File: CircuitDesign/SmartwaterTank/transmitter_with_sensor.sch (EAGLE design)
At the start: 11 parts, among them IC1 MEGA8-P

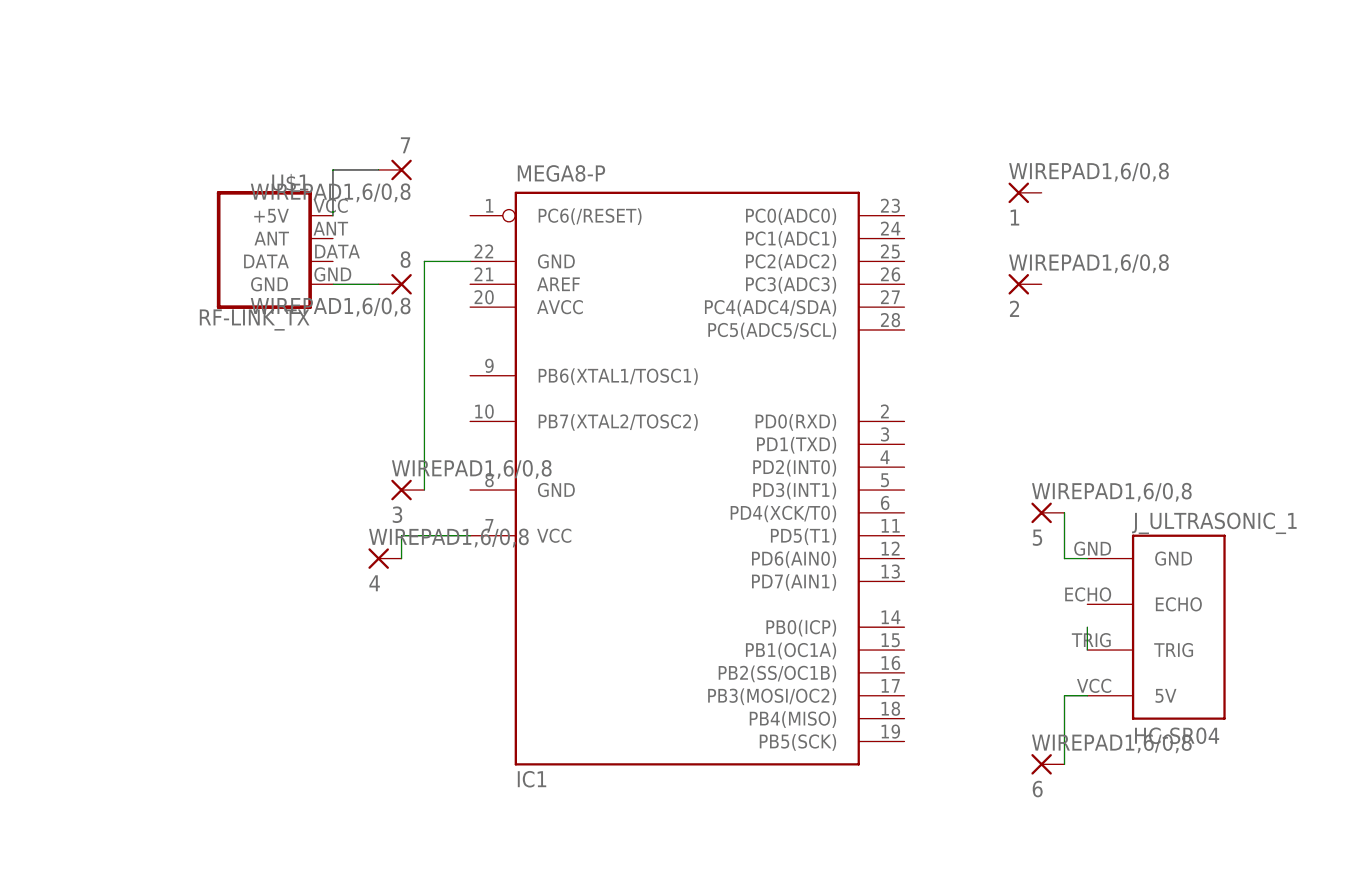
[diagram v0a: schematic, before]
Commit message: Issue #5: update transmitter schema
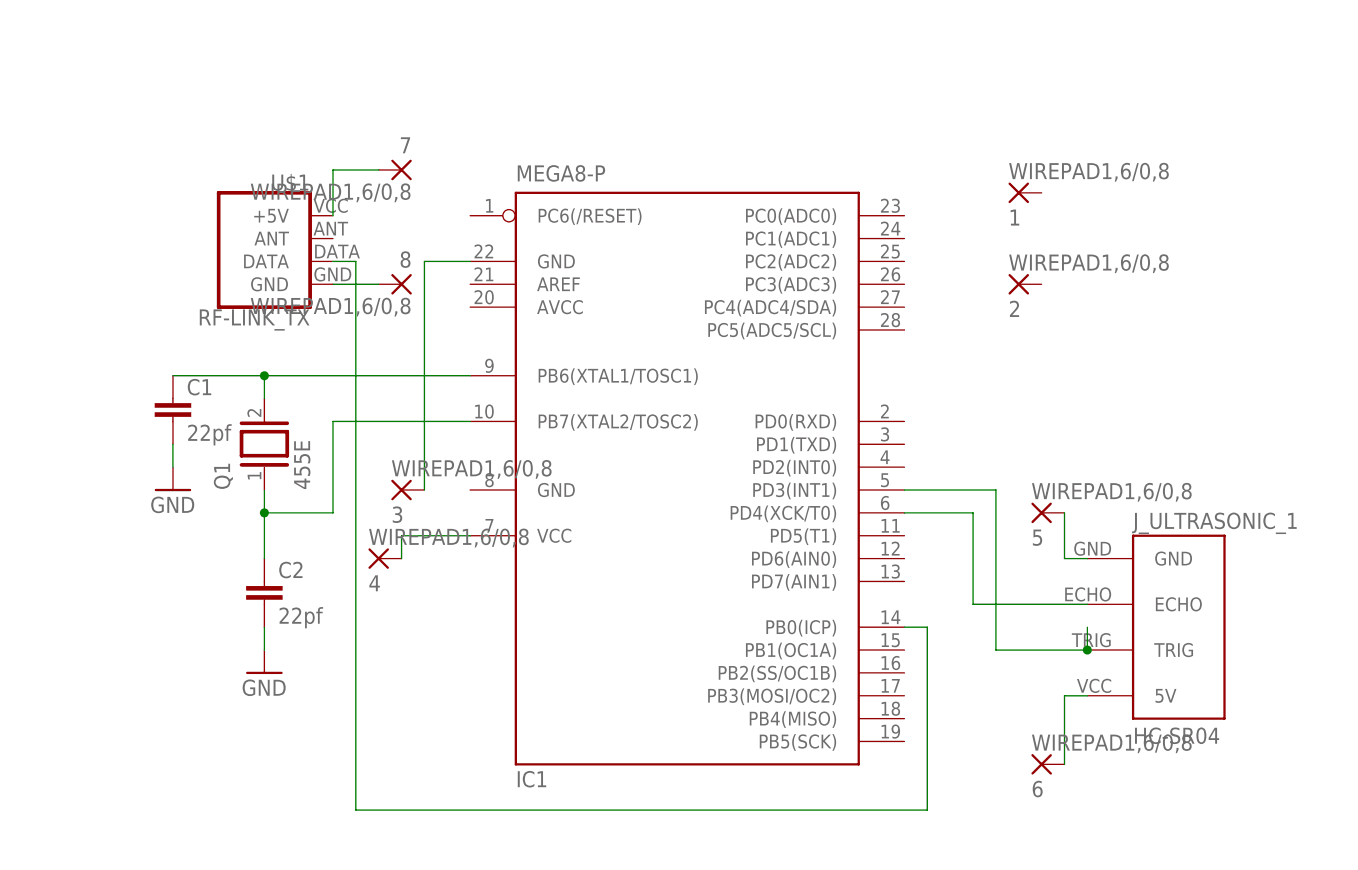
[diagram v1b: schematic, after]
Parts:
- added C1, C2: 22pf, rcl:C-EU025-025X050
- added Q1: 455E, special:XTAL/S
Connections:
- new net GND: C1.2, C2.2
- new net N$10: IC1.PD4(XCK/T0), J_ULTRASONIC_1.ECHO
- new net N$7: C1.1, IC1.PB6(XTAL1/TOSC1), Q1.2
- new net N$8: C2.1, IC1.PB7(XTAL2/TOSC2), Q1.1
- new net N$9: IC1.PB0(ICP), U$1.DATA
- net N$11: now also IC1.PD3(INT1)
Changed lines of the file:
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@@
 <part name="1" library="wirepad" library_urn="urn:adsk.eagle:library:412" deviceset="WIREPAD" device="1,6/0,8" package3d_urn="urn:adsk.eagle:package:30830/1"/>
 <part name="2" library="wirepad" library_urn="urn:adsk.eagle:library:412" deviceset="WIREPAD" device="1,6/0,8" package3d_urn="urn:adsk.eagle:package:30830/1"/>
+<part name="Q1" library="special" library_urn="urn:adsk.eagle:library:367" deviceset="XTAL/S" device="" package3d_urn="urn:adsk.eagle:package:26647/2" value="455E"/>
+<part name="C1" library="rcl" library_urn="urn:adsk.eagle:library:334" deviceset="C-EU" device="025-025X050" package3d_urn="urn:adsk.eagle:package:23629/2" value="22pf"/>
+<part name="C2" library="rcl" library_urn="urn:adsk.eagle:library:334" deviceset="C-EU" device="025-025X050" package3d_urn="urn:adsk.eagle:package:23629/2" value="22pf"/>
+<part name="GND1" library="supply1" library_urn="urn:adsk.eagle:library:371" deviceset="GND" device=""/>
+<part name="GND2" library="supply1" library_urn="urn:adsk.eagle:library:371" deviceset="GND" device=""/>
 </parts>
 <sheets>
@@
 <attribute name="VALUE" x="-11.303" y="115.062" size="1.778" layer="96" rot="MR180"/>
 </instance>
+<instance part="Q1" gate="G$1" x="-93.98" y="93.98" smashed="yes" rot="R90">
+<attribute name="NAME" x="-97.79" y="88.9" size="1.778" layer="95" rot="R90"/>
+<attribute name="VALUE" x="-88.9" y="88.9" size="1.778" layer="96" rot="R90"/>
+</instance>
+<instance part="C1" gate="G$1" x="-104.14" y="99.06" smashed="yes">
+<attribute name="NAME" x="-102.616" y="99.441" size="1.778" layer="95"/>
+<attribute name="VALUE" x="-102.616" y="94.361" size="1.778" layer="96"/>
+</instance>
+<instance part="C2" gate="G$1" x="-93.98" y="78.74" smashed="yes">
+<attribute name="NAME" x="-92.456" y="79.121" size="1.778" layer="95"/>
+<attribute name="VALUE" x="-92.456" y="74.041" size="1.778" layer="96"/>
+</instance>
+<instance part="GND1" gate="1" x="-93.98" y="68.58" smashed="yes">
+<attribute name="VALUE" x="-96.52" y="66.04" size="1.778" layer="96"/>
+</instance>
+<instance part="GND2" gate="1" x="-104.14" y="88.9" smashed="yes">
+<attribute name="VALUE" x="-106.68" y="86.36" size="1.778" layer="96"/>
+</instance>
 </instances>
 <busses>
@@
 <pinref part="J_ULTRASONIC_1" gate="J_ULTRASONIC" pin="TRIG"/>
 <wire x1="-2.54" y1="71.12" x2="-2.54" y2="73.66" width="0.1524" layer="91"/>
+<wire x1="-2.54" y1="71.12" x2="-12.7" y2="71.12" width="0.1524" layer="91"/>
+<junction x="-2.54" y="71.12"/>
+<wire x1="-12.7" y1="71.12" x2="-12.7" y2="88.9" width="0.1524" layer="91"/>
+<pinref part="IC1" gate="G$1" pin="PD3(INT1)"/>
+<wire x1="-12.7" y1="88.9" x2="-22.86" y2="88.9" width="0.1524" layer="91"/>
 </segment>
 </net>
@@
 <wire x1="-76.2" y1="88.9" x2="-76.2" y2="114.3" width="0.1524" layer="91"/>
 <wire x1="-76.2" y1="114.3" x2="-71.12" y2="114.3" width="0.1524" layer="91"/>
+</segment>
+</net>
+<net name="N$7" class="0">
+<segment>
+<pinref part="IC1" gate="G$1" pin="PB6(XTAL1/TOSC1)"/>
+<wire x1="-71.12" y1="101.6" x2="-93.98" y2="101.6" width="0.1524" layer="91"/>
+<pinref part="Q1" gate="G$1" pin="2"/>
+<wire x1="-93.98" y1="101.6" x2="-93.98" y2="99.06" width="0.1524" layer="91"/>
+<pinref part="C1" gate="G$1" pin="1"/>
+<wire x1="-93.98" y1="101.6" x2="-104.14" y2="101.6" width="0.1524" layer="91"/>
+<junction x="-93.98" y="101.6"/>
+</segment>
+</net>
+<net name="N$8" class="0">
+<segment>
+<pinref part="IC1" gate="G$1" pin="PB7(XTAL2/TOSC2)"/>
+<wire x1="-71.12" y1="96.52" x2="-86.36" y2="96.52" width="0.1524" layer="91"/>
+<wire x1="-86.36" y1="96.52" x2="-86.36" y2="86.36" width="0.1524" layer="91"/>
+<wire x1="-86.36" y1="86.36" x2="-93.98" y2="86.36" width="0.1524" layer="91"/>
+<pinref part="Q1" gate="G$1" pin="1"/>
+<wire x1="-93.98" y1="86.36" x2="-93.98" y2="88.9" width="0.1524" layer="91"/>
+<pinref part="C2" gate="G$1" pin="1"/>
+<wire x1="-93.98" y1="86.36" x2="-93.98" y2="81.28" width="0.1524" layer="91"/>
+<junction x="-93.98" y="86.36"/>
+</segment>
+</net>
+<net name="N$9" class="0">
+<segment>
+<pinref part="IC1" gate="G$1" pin="PB0(ICP)"/>
+<wire x1="-22.86" y1="73.66" x2="-20.32" y2="73.66" width="0.1524" layer="91"/>
+<wire x1="-20.32" y1="73.66" x2="-20.32" y2="53.34" width="0.1524" layer="91"/>
+<wire x1="-20.32" y1="53.34" x2="-83.82" y2="53.34" width="0.1524" layer="91"/>
+<pinref part="U$1" gate="G$1" pin="DATA"/>
+<wire x1="-83.82" y1="53.34" x2="-83.82" y2="114.3" width="0.1524" layer="91"/>
+<wire x1="-83.82" y1="114.3" x2="-86.36" y2="114.3" width="0.1524" layer="91"/>
+</segment>
+</net>
+<net name="N$10" class="0">
+<segment>
+<pinref part="IC1" gate="G$1" pin="PD4(XCK/T0)"/>
+<wire x1="-22.86" y1="86.36" x2="-15.24" y2="86.36" width="0.1524" layer="91"/>
+<wire x1="-15.24" y1="86.36" x2="-15.24" y2="76.2" width="0.1524" layer="91"/>
+<pinref part="J_ULTRASONIC_1" gate="J_ULTRASONIC" pin="ECHO"/>
+<wire x1="-15.24" y1="76.2" x2="-2.54" y2="76.2" width="0.1524" layer="91"/>
+</segment>
+</net>
+<net name="GND" class="0">
+<segment>
+<pinref part="C1" gate="G$1" pin="2"/>
+<pinref part="GND2" gate="1" pin="GND"/>
+<wire x1="-104.14" y1="93.98" x2="-104.14" y2="91.44" width="0.1524" layer="91"/>
+</segment>
+<segment>
+<pinref part="C2" gate="G$1" pin="2"/>
+<pinref part="GND1" gate="1" pin="GND"/>
+<wire x1="-93.98" y1="73.66" x2="-93.98" y2="71.12" width="0.1524" layer="91"/>
 </segment>
 </net>
@@
 packages will not be understood (or retained) with this version.
 </note>
+<note version="8.4" severity="warning">
+Since Version 8.4, EAGLE supports properties for SPICE simulation.
+Probes in schematics and SPICE mapping objects found in parts and library devices
+will not be understood with this version. Update EAGLE to the latest version
+for full support of SPICE simulation.
+</note>
 </compatibility>

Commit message: Issue #2: complete transmitter board design for vero board
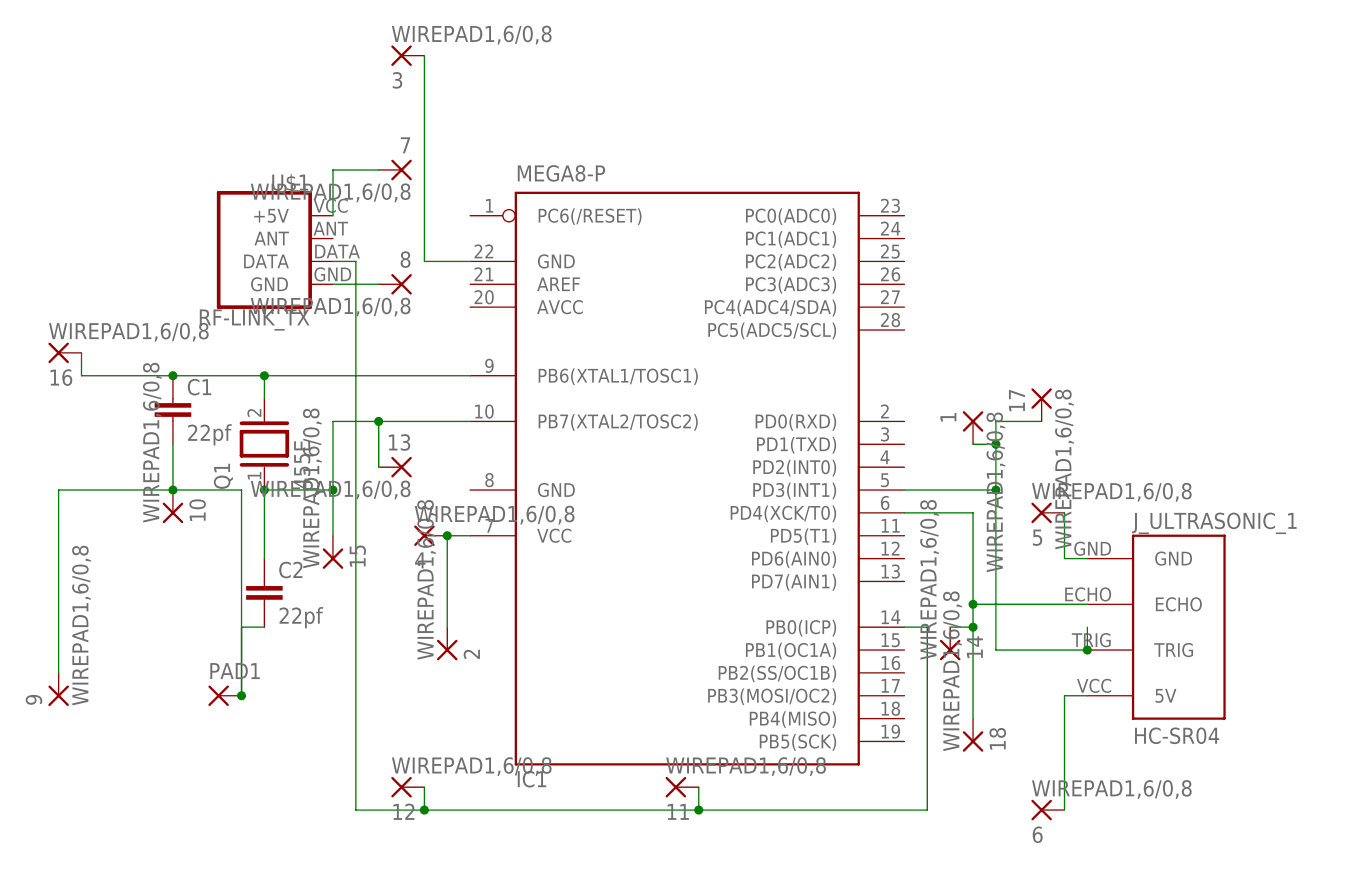
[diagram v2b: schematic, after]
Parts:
- added 10, 11, 12, 13, 14, 15, 16, 17, 18, 9: WIREPAD1,6/0,8, wirepad:WIREPAD1,6/0,8
- added PAD1: (no value), wirepad:1,6/0,8
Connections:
- removed net GND: C1.2, C2.2
- removed net N$9: IC1.PB0(ICP), U$1.DATA
- new net N$12: 10.P, 9.P, C1.2, C2.2, PAD1.P
- new net N$14: 11.P, 12.P, IC1.PB0(ICP), U$1.DATA
- net N$10: now also 14.P, 18.P
- net N$11: now also 1.P, 17.P
- net N$3: now also 2.P
- net N$7: now also 16.P
- net N$8: now also 13.P, 15.P
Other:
- moved on the sheet: 1, 2, 3, 4, 6

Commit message: Issue #2: remove unnecessary texts from schematic
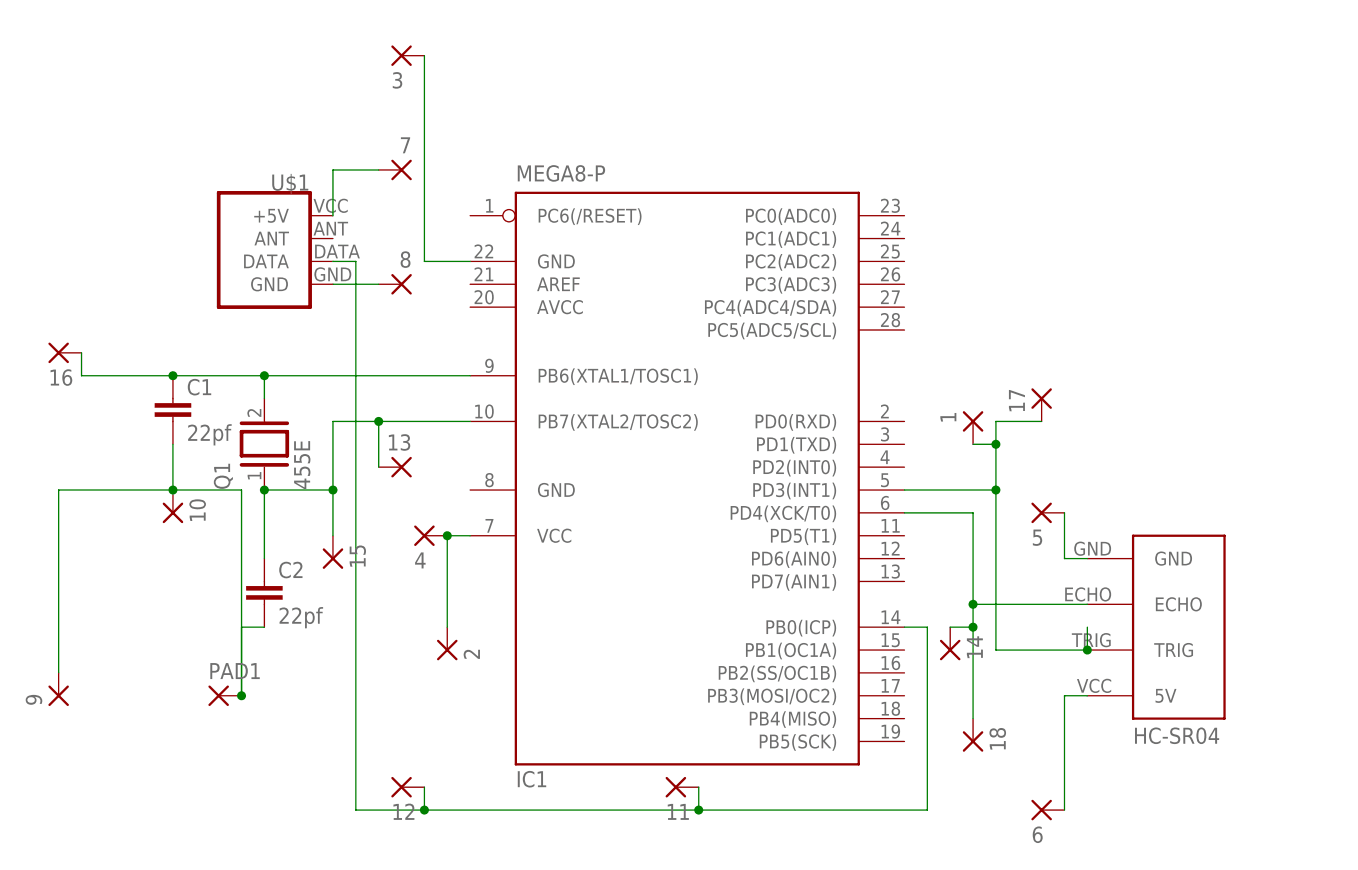
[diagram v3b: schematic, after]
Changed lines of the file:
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@@
 <instance part="U$1" gate="G$1" x="-93.98" y="114.3" smashed="yes" rot="MR0">
 <attribute name="NAME" x="-88.9" y="122.174" size="1.778" layer="95" font="vector" rot="MR0"/>
-<attribute name="VALUE" x="-88.9" y="108.966" size="1.778" layer="96" font="vector" rot="MR0" align="top-left"/>
 </instance>
 <instance part="J_ULTRASONIC_1" gate="J_ULTRASONIC" x="10.16" y="73.66" smashed="yes">
-<attribute name="NAME" x="2.54" y="84.582" size="1.778" layer="95" ratio="12"/>
 <attribute name="VALUE" x="2.54" y="60.706" size="1.778" layer="96" ratio="12"/>
 </instance>
 <instance part="3" gate="G$1" x="-78.74" y="137.16" smashed="yes" rot="MR180">
 <attribute name="NAME" x="-79.883" y="135.3058" size="1.778" layer="95" rot="MR180"/>
-<attribute name="VALUE" x="-79.883" y="140.462" size="1.778" layer="96" rot="MR180"/>
 </instance>
 <instance part="4" gate="G$1" x="-76.2" y="83.82" smashed="yes" rot="MR180">
 <attribute name="NAME" x="-77.343" y="81.9658" size="1.778" layer="95" rot="MR180"/>
-<attribute name="VALUE" x="-77.343" y="87.122" size="1.778" layer="96" rot="MR180"/>
 </instance>
 <instance part="5" gate="G$1" x="-7.62" y="86.36" smashed="yes" rot="MR180">
 <attribute name="NAME" x="-8.763" y="84.5058" size="1.778" layer="95" rot="MR180"/>
-<attribute name="VALUE" x="-8.763" y="89.662" size="1.778" layer="96" rot="MR180"/>
 </instance>
 <instance part="6" gate="G$1" x="-7.62" y="53.34" smashed="yes" rot="MR180">
 <attribute name="NAME" x="-8.763" y="51.4858" size="1.778" layer="95" rot="MR180"/>
-<attribute name="VALUE" x="-8.763" y="56.642" size="1.778" layer="96" rot="MR180"/>
 </instance>
 <instance part="7" gate="G$1" x="-78.74" y="124.46" smashed="yes" rot="MR0">
 <attribute name="NAME" x="-77.597" y="126.3142" size="1.778" layer="95" rot="MR0"/>
-<attribute name="VALUE" x="-77.597" y="121.158" size="1.778" layer="96" rot="MR0"/>
 </instance>
 <instance part="8" gate="G$1" x="-78.74" y="111.76" smashed="yes" rot="MR0">
 <attribute name="NAME" x="-77.597" y="113.6142" size="1.778" layer="95" rot="MR0"/>
-<attribute name="VALUE" x="-77.597" y="108.458" size="1.778" layer="96" rot="MR0"/>
 </instance>
 <instance part="1" gate="G$1" x="-15.24" y="96.52" smashed="yes" rot="MR270">
 <attribute name="NAME" x="-17.0942" y="97.663" size="1.778" layer="95" rot="MR270"/>
-<attribute name="VALUE" x="-11.938" y="97.663" size="1.778" layer="96" rot="MR270"/>
 </instance>
 <instance part="2" gate="G$1" x="-73.66" y="71.12" smashed="yes" rot="MR90">
 <attribute name="NAME" x="-71.8058" y="69.977" size="1.778" layer="95" rot="MR90"/>
-<attribute name="VALUE" x="-76.962" y="69.977" size="1.778" layer="96" rot="MR90"/>
 </instance>
 <instance part="Q1" gate="G$1" x="-93.98" y="93.98" smashed="yes" rot="R90">
@@
 <instance part="9" gate="G$1" x="-116.84" y="66.04" smashed="yes" rot="R90">
 <attribute name="NAME" x="-118.6942" y="64.897" size="1.778" layer="95" rot="R90"/>
-<attribute name="VALUE" x="-113.538" y="64.897" size="1.778" layer="96" rot="R90"/>
 </instance>
 <instance part="10" gate="G$1" x="-104.14" y="86.36" smashed="yes" rot="MR90">
 <attribute name="NAME" x="-102.2858" y="85.217" size="1.778" layer="95" rot="MR90"/>
-<attribute name="VALUE" x="-107.442" y="85.217" size="1.778" layer="96" rot="MR90"/>
 </instance>
 <instance part="PAD1" gate="P" x="-99.06" y="66.04" smashed="yes">
@@
 <instance part="11" gate="G$1" x="-48.26" y="55.88" smashed="yes" rot="MR180">
 <attribute name="NAME" x="-49.403" y="54.0258" size="1.778" layer="95" rot="MR180"/>
-<attribute name="VALUE" x="-49.403" y="59.182" size="1.778" layer="96" rot="MR180"/>
 </instance>
 <instance part="12" gate="G$1" x="-78.74" y="55.88" smashed="yes" rot="MR180">
 <attribute name="NAME" x="-79.883" y="54.0258" size="1.778" layer="95" rot="MR180"/>
-<attribute name="VALUE" x="-79.883" y="59.182" size="1.778" layer="96" rot="MR180"/>
 </instance>
 <instance part="13" gate="G$1" x="-78.74" y="91.44" smashed="yes" rot="MR0">
 <attribute name="NAME" x="-77.597" y="93.2942" size="1.778" layer="95" rot="MR0"/>
-<attribute name="VALUE" x="-77.597" y="88.138" size="1.778" layer="96" rot="MR0"/>
 </instance>
 <instance part="14" gate="G$1" x="-17.78" y="71.12" smashed="yes" rot="MR90">
 <attribute name="NAME" x="-15.9258" y="69.977" size="1.778" layer="95" rot="MR90"/>
-<attribute name="VALUE" x="-21.082" y="69.977" size="1.778" layer="96" rot="MR90"/>
 </instance>
 <instance part="15" gate="G$1" x="-86.36" y="81.28" smashed="yes" rot="MR90">
 <attribute name="NAME" x="-84.5058" y="80.137" size="1.778" layer="95" rot="MR90"/>
-<attribute name="VALUE" x="-89.662" y="80.137" size="1.778" layer="96" rot="MR90"/>
 </instance>
 <instance part="16" gate="G$1" x="-116.84" y="104.14" smashed="yes" rot="MR180">
 <attribute name="NAME" x="-117.983" y="102.2858" size="1.778" layer="95" rot="MR180"/>
-<attribute name="VALUE" x="-117.983" y="107.442" size="1.778" layer="96" rot="MR180"/>
 </instance>
 <instance part="17" gate="G$1" x="-7.62" y="99.06" smashed="yes" rot="MR270">
 <attribute name="NAME" x="-9.4742" y="100.203" size="1.778" layer="95" rot="MR270"/>
-<attribute name="VALUE" x="-4.318" y="100.203" size="1.778" layer="96" rot="MR270"/>
 </instance>
 <instance part="18" gate="G$1" x="-15.24" y="60.96" smashed="yes" rot="MR90">
 <attribute name="NAME" x="-13.3858" y="59.817" size="1.778" layer="95" rot="MR90"/>
-<attribute name="VALUE" x="-18.542" y="59.817" size="1.778" layer="96" rot="MR90"/>
 </instance>
 </instances>

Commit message: Issue #2: update schema and board
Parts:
- removed 10, 13, 15, 16, 9: WIREPAD1,6/0,8, wirepad:WIREPAD1,6/0,8
- removed C1, C2: 22pf, rcl:C-EU025-025X050
- removed PAD1: (no value), wirepad:1,6/0,8
- removed Q1: 455E, special:XTAL/S
- added 19, 20, G, MISO, MOSI, RESET, SCK: WIREPAD1,6/0,8, wirepad:WIREPAD1,6/0,8
- added Y1: 32.768kHz, SparkFun-Clocks:CRYSTAL-32.768KHZPTH-2X6
- renumbered 12 to DATA, 17 to TRIG, 18 to ECHO, 2 to V, 3 to G2
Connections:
- new net N$13: IC1.PB4(MISO), MISO.P
- new net N$15: IC1.PB5(SCK), SCK.P
- new net N$9: 19.P, 20.P, IC1.PC6(/RESET), RESET.P
- net N$12: now also IC1.PB3(MOSI/OC2), MOSI.P; no longer 10.P, 9.P, C1.2, C2.2, PAD1.P
- net N$2: now also G.P
- net N$7: now also Y1.2; no longer 16.P, C1.1, Q1.2
- net N$8: now also Y1.1; no longer 13.P, 15.P, C2.1, Q1.1
